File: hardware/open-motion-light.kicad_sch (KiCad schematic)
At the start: 79 parts, among them J1 TYPE-C-31-M-12, J2 Conn_01x04, Q1 2N7002, SW1 SW_Push, SW2 SW_Push, SW3 SSSS213800, U1 CN3058E, U2 STM32L031G6U6, U3 MT9284BS6, U4 PIR223D-S0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

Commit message: Start placing components
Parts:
- J1: footprint homebrew:HRO_TYPE-C-31-M-12 -> Homebrew:HRO_TYPE-C-31-M-12
- SW1, SW2: footprint Button_Switch_SMD:SW_Push_1P1T_XKB_TS-1187A -> Homebrew:SW_TACTILE_5.1MM_TS-1187A-C-D-B
- U1: footprint homebrew:SOP-8_3.9x4.9mm_P1.27mm_Thermal -> Homebrew:SOP-8_3.9x4.9mm_P1.27mm_Thermal
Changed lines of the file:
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@@
 			)
 		)
-		(property "Footprint" "homebrew:HRO_TYPE-C-31-M-12"
+		(property "Footprint" "Homebrew:HRO_TYPE-C-31-M-12"
 			(at 57.15 248.92 0)
 			(effects
@@
 			)
 		)
-		(property "Footprint" "homebrew:SOP-8_3.9x4.9mm_P1.27mm_Thermal"
+		(property "Footprint" "Homebrew:SOP-8_3.9x4.9mm_P1.27mm_Thermal"
 			(at 59.69 190.5 0)
 			(effects
@@
 			)
 		)
-		(property "Footprint" "Button_Switch_SMD:SW_Push_1P1T_XKB_TS-1187A"
+		(property "Footprint" "Homebrew:SW_TACTILE_5.1MM_TS-1187A-C-D-B"
 			(at 162.56 31.75 0)
 			(effects
@@
 			)
 		)
-		(property "Footprint" "Button_Switch_SMD:SW_Push_1P1T_XKB_TS-1187A"
+		(property "Footprint" "Homebrew:SW_TACTILE_5.1MM_TS-1187A-C-D-B"
 			(at 21.59 30.48 0)
 			(effects

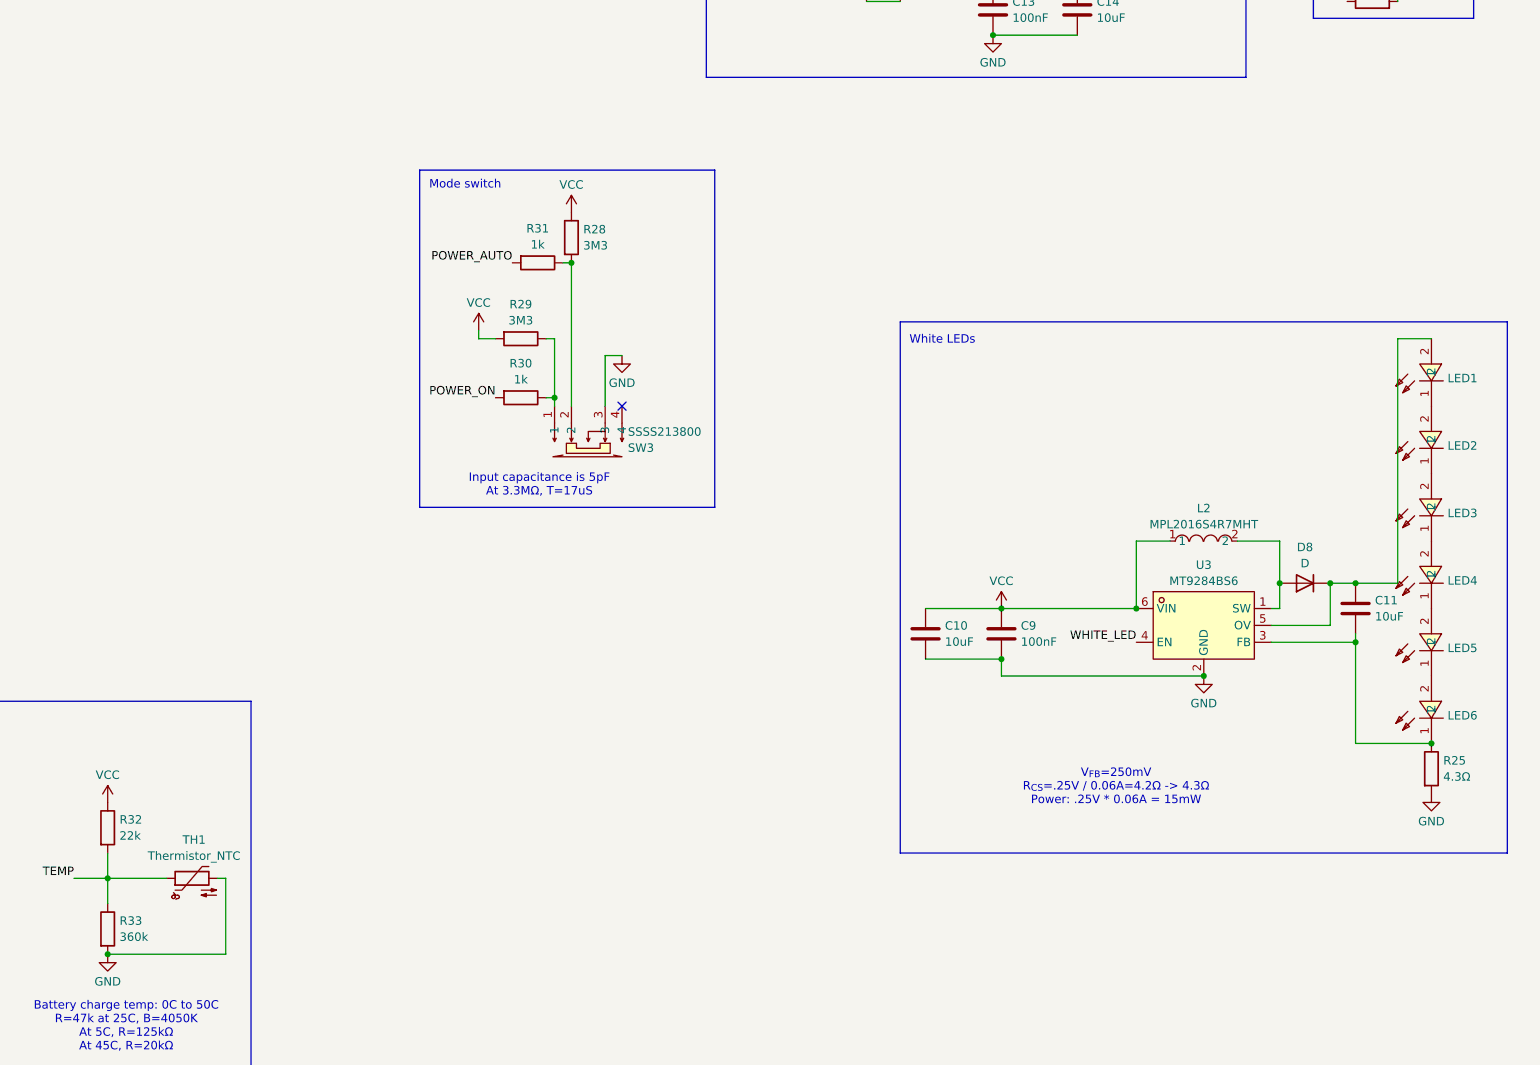
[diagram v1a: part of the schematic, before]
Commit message: Migrate three resistors to basic components, continue placement
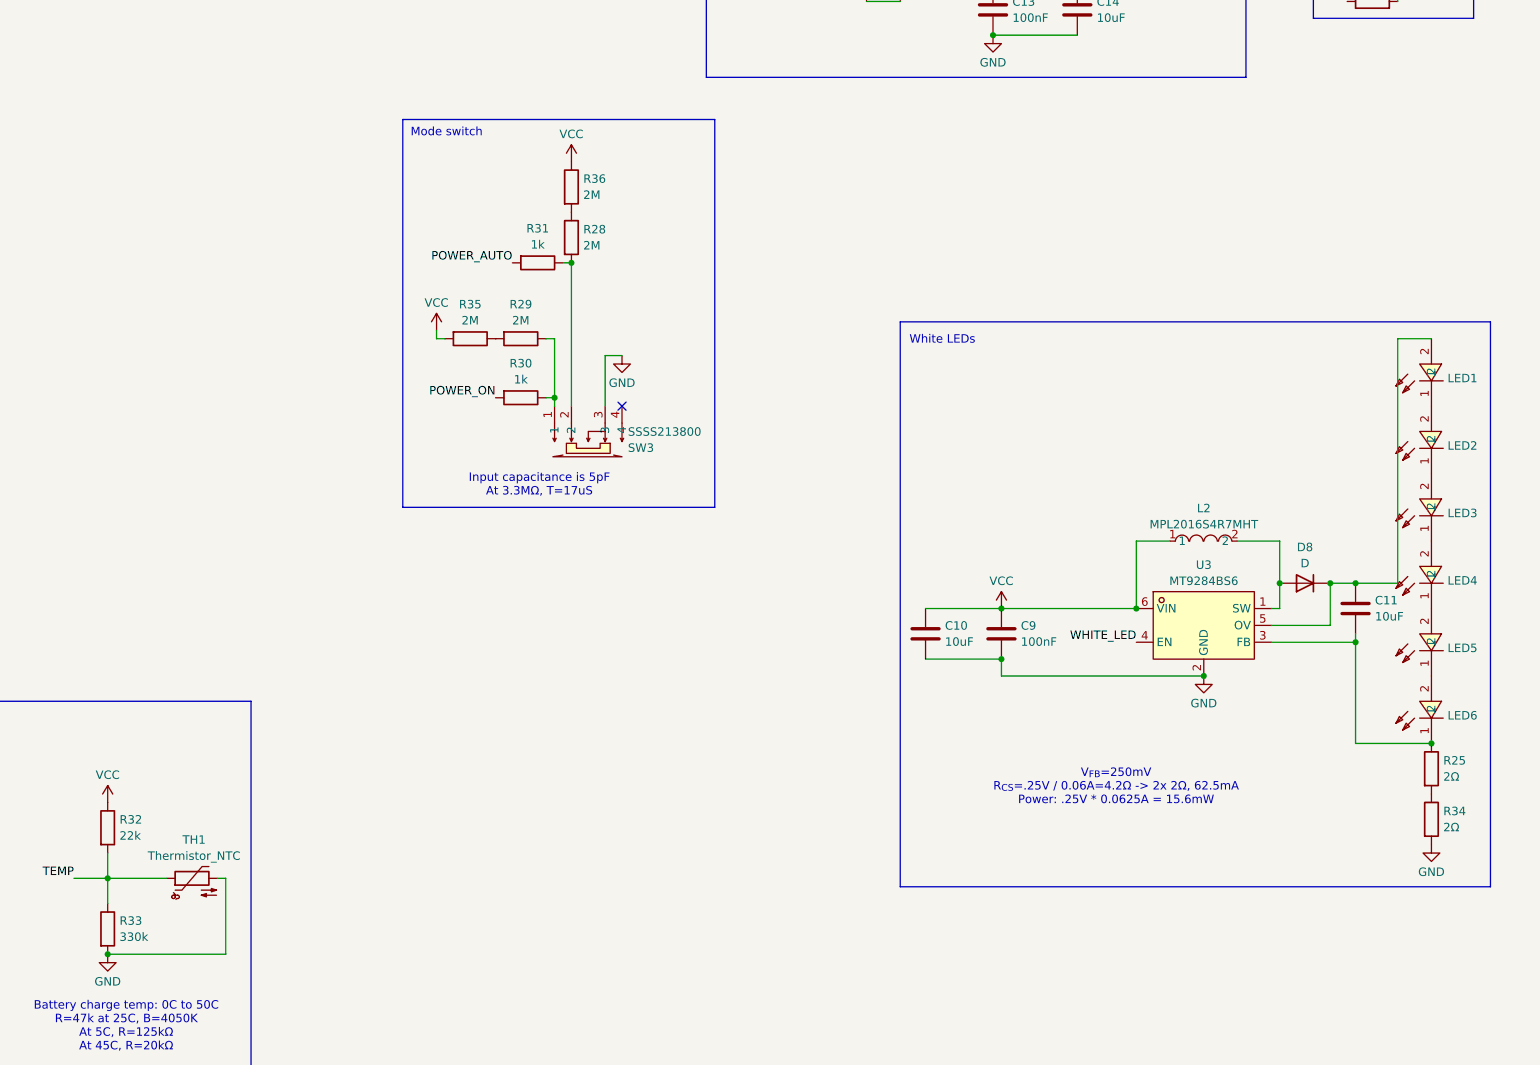
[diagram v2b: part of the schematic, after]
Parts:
- added R34: 2Ω, Resistor_SMD:R_0603_1608Metric, symbol Device:R
- added R35, R36: 2M, Resistor_SMD:R_0603_1608Metric, symbol Device:R
- R1, R2: footprint Resistor_SMD:R_0402_1005Metric -> Resistor_SMD:R_0603_1608Metric
- R25: value 4.3Ω -> 2Ω; LCSC C23161 -> C22977
- R28, R29: value 3M3 -> 2M; footprint Resistor_SMD:R_0402_1005Metric -> Resistor_SMD:R_0603_1608Metric; LCSC C270613 -> C22976
- R33: value 360k -> 330k; footprint Resistor_SMD:R_0402_1005Metric -> Resistor_SMD:R_0603_1608Metric; LCSC C45956 -> C23137
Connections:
- net GND: now also R34.2; no longer R25.2
- net VCC: now also R35.2, R36.1; no longer R28.1, R29.2
- new net: R28.1, R36.2
- new net: R25.2, R34.1
- new net: R29.2, R35.1
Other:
- note added: "V_{FB}=250mV R_{CS}=.25V / 0.06A=4.2Ω -> 2x 2Ω, 62.5mA Power: .25V * 0.0625A = 15.6mW"
- note removed: "V_{FB}=250mV R_{CS}=.25V / 0.06A=4.2Ω -> 4.3Ω Power: .25V * 0.06A = 15mW"

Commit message: Continue placement
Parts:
- removed C14: 10uF, Capacitor_SMD:C_0603_1608Metric, symbol Device:C
- removed U5: LTR-553ALS-01, easyeda2kicad:SENSOR-SMD_L3.9-W2.4-P0.95-BL, symbol Homebrew:LTR-553ALS-01
- added C18: 100nF, Capacitor_SMD:C_0402_1005Metric, symbol Device:C
- added C19: 47uF, Capacitor_SMD:C_1206_3216Metric, symbol Device:C
- added C20: 10uF, Capacitor_SMD:C_0603_1608Metric, symbol Device:C
- added H1, H2, H3: MountingHole, MountingHole:MountingHole_3.2mm_M3_ISO7380, symbol Mechanical:MountingHole
- added R37: 10, Resistor_SMD:R_0402_1005Metric, symbol Device:R
- added U5: VCNL4010-GS08, easyeda2kicad:SENSORS-SMD_VCNL4010-GS08, symbol Homebrew:VCNL4010-GS08
- BT1: footprint easyeda2kicad:BAT-TH_BH-18650-A1AJ005 -> Homebrew:BAT-TH_BH-18650-A1AJ005
- C11: value 10uF -> 10uF 28V; footprint Capacitor_SMD:C_0603_1608Metric -> Capacitor_SMD:C_1206_3216Metric
- C13: value 100nF -> 47uF; footprint Capacitor_SMD:C_0402_1005Metric -> Capacitor_SMD:C_1206_3216Metric; LCSC C307331 -> C96123
- R18: value 4k7 -> 100k; LCSC C25900 -> C25741
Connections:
- net GND: now also C12.1, C13.1, U4.3 (VSS), C18.1, C19.1, C20.2, U5.12 (GND), U5.13 (GND); no longer C12.2, C13.2, U4. (VSS)
- net SCL: now also U5.5 (SCL)
- net SDA: now also R20.2, U5.4 (SDA); no longer R18.2
- net VCC: now also C13.2, U4.1 (VDD), C18.2, C19.2, R37.1, U5.1 (IR_anode); no longer C12.1, C13.1, R8.2, R9.2, U4. (VSS)
- net at R17.2: now also U4.2 (RELOUT); no longer U4. (VSS)
- net at R27.1: now also R18.2, U5.6 (INT); no longer R20.2
- net at R7.2, U1.6 (~{DONE}): now also R8.2
- net at R6.2, U1.7 (~{CHRG}): now also R9.2
- new net: C12.2, C20.1, R37.2, U5.7 (VDD)
- no-connect marks 6 -> 8
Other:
- note added: "V_{Fmax}=3.2V @ 60mA V_{LEDSmax}=19V Overvoltage protection: 28V"
- moved on the sheet: C12, LED1, LED2, LED3, LED4, LED5, LED6, R17, R18, R19, R20, R25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

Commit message: Finish placement
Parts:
- L2: footprint easyeda2kicad:L0806 -> Homebrew:L0806
- LED1, LED2, LED3, LED4, LED5, LED6: footprint easyeda2kicad:LED-SMD_L3.3-W2.8-RD -> Homebrew:LED-SMD_L3.3-W2.8-RD
- SW3: footprint easyeda2kicad:SW-SMD_SSSS213800 -> Homebrew:SW-SMD_SSSS213800
- U3: footprint easyeda2kicad:SOT-23-6_L2.9-W1.6-P0.95-LS2.8-BR -> Homebrew:SOT-23-6_L2.9-W1.6-P0.95-LS2.8-BR
- U5: footprint easyeda2kicad:SENSORS-SMD_VCNL4010-GS08 -> Homebrew:SENSORS-SMD_VCNL4010-GS08
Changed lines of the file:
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@@
 			)
 		)
-		(property "Footprint" "easyeda2kicad:L0806"
+		(property "Footprint" "Homebrew:L0806"
 			(at 332.74 134.62 0)
 			(effects
@@
 			)
 		)
-		(property "Footprint" "easyeda2kicad:LED-SMD_L3.3-W2.8-RD"
+		(property "Footprint" "Homebrew:LED-SMD_L3.3-W2.8-RD"
 			(at 378.46 101.6 0)
 			(effects
@@
 			)
 		)
-		(property "Footprint" "easyeda2kicad:LED-SMD_L3.3-W2.8-RD"
+		(property "Footprint" "Homebrew:LED-SMD_L3.3-W2.8-RD"
 			(at 378.46 111.76 0)
 			(effects
@@
 			)
 		)
-		(property "Footprint" "easyeda2kicad:LED-SMD_L3.3-W2.8-RD"
+		(property "Footprint" "Homebrew:LED-SMD_L3.3-W2.8-RD"
 			(at 378.46 142.24 0)
 			(effects
@@
 			)
 		)
-		(property "Footprint" "easyeda2kicad:LED-SMD_L3.3-W2.8-RD"
+		(property "Footprint" "Homebrew:LED-SMD_L3.3-W2.8-RD"
 			(at 378.46 121.92 0)
 			(effects
@@
 			)
 		)
-		(property "Footprint" "easyeda2kicad:LED-SMD_L3.3-W2.8-RD"
+		(property "Footprint" "Homebrew:LED-SMD_L3.3-W2.8-RD"
 			(at 378.46 132.08 0)
 			(effects
@@
 			)
 		)
-		(property "Footprint" "easyeda2kicad:SW-SMD_SSSS213800"
+		(property "Footprint" "Homebrew:SW-SMD_SSSS213800"
 			(at 240.03 99.06 0)
 			(effects
@@
 			)
 		)
-		(property "Footprint" "easyeda2kicad:SOT-23-6_L2.9-W1.6-P0.95-LS2.8-BR"
+		(property "Footprint" "Homebrew:SOT-23-6_L2.9-W1.6-P0.95-LS2.8-BR"
 			(at 332.994 128.016 0)
 			(effects
@@
 			)
 		)
-		(property "Footprint" "easyeda2kicad:LED-SMD_L3.3-W2.8-RD"
+		(property "Footprint" "Homebrew:LED-SMD_L3.3-W2.8-RD"
 			(at 378.46 152.4 0)
 			(effects
@@
 			)
 		)
-		(property "Footprint" "easyeda2kicad:SENSORS-SMD_VCNL4010-GS08"
+		(property "Footprint" "Homebrew:SENSORS-SMD_VCNL4010-GS08"
 			(at 315.722 29.21 0)
 			(effects

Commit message: First pass at routing
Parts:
- added C14: 100nF, Capacitor_SMD:C_0402_1005Metric, symbol Device:C
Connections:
- net GND: now also U1.9 (EP), C14.2
- net VCC: now also C14.1
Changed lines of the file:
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@@
 	)
 	(junction
+		(at 59.69 191.77)
+		(diameter 0)
+		(color 0 0 0 0)
+	)
+	(junction
 		(at 59.69 158.75)
 		(diameter 0)
@@
 	)
 	(junction
+		(at 152.4 76.2)
+		(diameter 0)
+		(color 0 0 0 0)
+	)
+	(junction
 		(at 350.52 46.99)
 		(diameter 0)
@@
 	(wire
 		(pts
+			(xy 59.69 191.77) (xy 60.96 191.77)
+		)
+		(stroke
+			(width 0)
+			(type default)
+		)
+	)
+	(wire
+		(pts
 			(xy 93.98 27.94) (xy 106.68 27.94)
 		)
@@
 	(wire
 		(pts
+			(xy 163.83 76.2) (xy 163.83 83.82)
+		)
+		(stroke
+			(width 0)
+			(type default)
+		)
+	)
+	(wire
+		(pts
 			(xy 302.26 144.78) (xy 302.26 147.32)
 		)
@@
 	(polyline
 		(pts
-			(xy 182.88 93.98) (xy 158.75 93.98)
+			(xy 182.88 93.98) (xy 149.86 93.98)
 		)
 		(stroke
@@
 	(polyline
 		(pts
-			(xy 158.75 63.5) (xy 182.88 63.5)
+			(xy 149.86 63.5) (xy 182.88 63.5)
 		)
 		(stroke
@@
 	(wire
 		(pts
+			(xy 152.4 76.2) (xy 163.83 76.2)
+		)
+		(stroke
+			(width 0)
+			(type default)
+		)
+	)
+	(wire
+		(pts
 			(xy 185.42 189.23) (xy 185.42 177.8)
 		)
@@
 	(polyline
 		(pts
-			(xy 158.75 63.5) (xy 158.75 93.98)
+			(xy 149.86 63.5) (xy 149.86 93.98)
 		)
 		(stroke
@@
 	(wire
 		(pts
+			(xy 58.42 191.77) (xy 59.69 191.77)
+		)
+		(stroke
+			(width 0)
+			(type default)
+		)
+	)
+	(wire
+		(pts
 			(xy 58.42 30.48) (xy 60.96 30.48)
 		)
@@
 	)
 	(symbol
+		(lib_id "Device:C")
+		(at 152.4 80.01 0)
+		(unit 1)
+		(exclude_from_sim no)
+		(in_bom yes)
+		(on_board yes)
+		(dnp no)
+		(fields_autoplaced yes)
+		(property "Reference" "C14"
+			(at 155.321 78.7978 0)
+			(effects
+				(font
+					(size 1.27 1.27)
+				)
+				(justify left)
+			)
+		)
+		(property "Value" "100nF"
+			(at 155.321 81.2221 0)
+			(effects
+				(font
+					(size 1.27 1.27)
+				)
+				(justify left)
+			)
+		)
+		(property "Footprint" "Capacitor_SMD:C_0402_1005Metric"
+			(at 153.3652 83.82 0)
+			(effects
+				(font
+					(size 1.27 1.27)
+				)
+				(hide yes)
+			)
+		)
+		(property "Datasheet" "~"
+			(at 152.4 80.01 0)
+			(effects
+				(font
+					(size 1.27 1.27)
+				)
+				(hide yes)
+			)
+		)
+		(property "Description" "Unpolarized capacitor"
+			(at 152.4 80.01 0)
+			(effects
+				(font
+					(size 1.27 1.27)
+				)
+				(hide yes)
+			)
+		)
+		(property "LCSC" "C307331"
+			(at 152.4 80.01 0)
+			(effects
+				(font
+					(size 1.27 1.27)
+				)
+				(hide yes)
+			)
+		)
+		(pin "2"
+		)
+		(pin "1"
+		)
+		(instances
+			(project "open-motion-light"
+				(path "/f39d6745-1b59-458d-9712-dda63c04ccc8"
+					(reference "C14")
+					(unit 1)
+				)
+			)
+		)
+	)
+	(symbol
 		(lib_id "Homebrew:MPL2016S4R7MHT")
 		(at 332.74 127 0)
@@
 	)
 	(symbol
+		(lib_id "power:GND")
+		(at 152.4 83.82 0)
+		(unit 1)
+		(exclude_from_sim no)
+		(in_bom yes)
+		(on_board yes)
+		(dnp no)
+		(fields_autoplaced yes)
+		(property "Reference" "#PWR028"
+			(at 152.4 90.17 0)
+			(effects
+				(font
+					(size 1.27 1.27)
+				)
+				(hide yes)
+			)
+		)
+		(property "Value" "GND"
+			(at 152.4 87.9531 0)
+			(effects
+				(font
+					(size 1.27 1.27)
+				)
+			)
+		)
+		(property "Footprint" ""
+			(at 152.4 83.82 0)
+			(effects
+				(font
+					(size 1.27 1.27)
+				)
+				(hide yes)
+			)
+		)
+		(property "Datasheet" ""
+			(at 152.4 83.82 0)
+			(effects
+				(font
+					(size 1.27 1.27)
+				)
+				(hide yes)
+			)
+		)
+		(property "Description" "Power symbol creates a global label with name \"GND\" , ground"
+			(at 152.4 83.82 0)
+			(effects
+				(font
+					(size 1.27 1.27)
+				)
+				(hide yes)
+			)
+		)
+		(pin "1"
+		)
+		(instances
+			(project "open-motion-light"
+				(path "/f39d6745-1b59-458d-9712-dda63c04ccc8"
+					(reference "#PWR028")
+					(unit 1)
+				)
+			)
+		)
+	)
+	(symbol
 		(lib_id "power:VCC")
 		(at 217.17 95.25 0)
@@
 			)
 		)
-		(property "Datasheet" "https://www.mikrocontroller.net/attachment/519010/DSE-CN3058E.pdf"
+		(property "Datasheet" "http://www.consonance-elec.com/pdf/datasheet/DSE-CN3058E.pdf"
 			(at 59.69 190.5 0)
 			(effects
@@
 		(pin "3"
 		)
+		(pin "9"
+		)
 		(instances
 			(project "open-motion-light"
@@
 	(symbol
 		(lib_id "power:VCC")
-		(at 163.83 83.82 0)
+		(at 152.4 76.2 0)
 		(unit 1)
 		(exclude_from_sim no)
@@
 		(fields_autoplaced yes)
 		(property "Reference" "#PWR024"
-			(at 163.83 87.63 0)
+			(at 152.4 80.01 0)
 			(effects
 				(font
@@
 		)
 		(property "Value" "VCC"
-			(at 163.83 79.6869 0)
+			(at 152.4 72.0669 0)
 			(effects
 				(font
@@
 		)
 		(property "Footprint" ""
-			(at 163.83 83.82 0)
+			(at 152.4 76.2 0)
 			(effects
 				(font
@@
 		)
 		(property "Datasheet" ""
-			(at 163.83 83.82 0)
+			(at 152.4 76.2 0)
 			(effects
 				(font
@@
 		)
 		(property "Description" "Power symbol creates a global label with name \"VCC\""
-			(at 163.83 83.82 0)
+			(at 152.4 76.2 0)
 			(effects
 				(font

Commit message: Hardware revision v1.0
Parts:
- C11: LCSC C96446 -> C13585
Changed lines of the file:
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@@
 			)
 		)
-		(property "LCSC" "C96446"
+		(property "LCSC" "C13585"
 			(at 355.6 137.16 0)
 			(effects
